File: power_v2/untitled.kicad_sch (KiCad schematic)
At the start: 15 parts, among them Q2 C1815_SOT23, U7 NEO-M8M

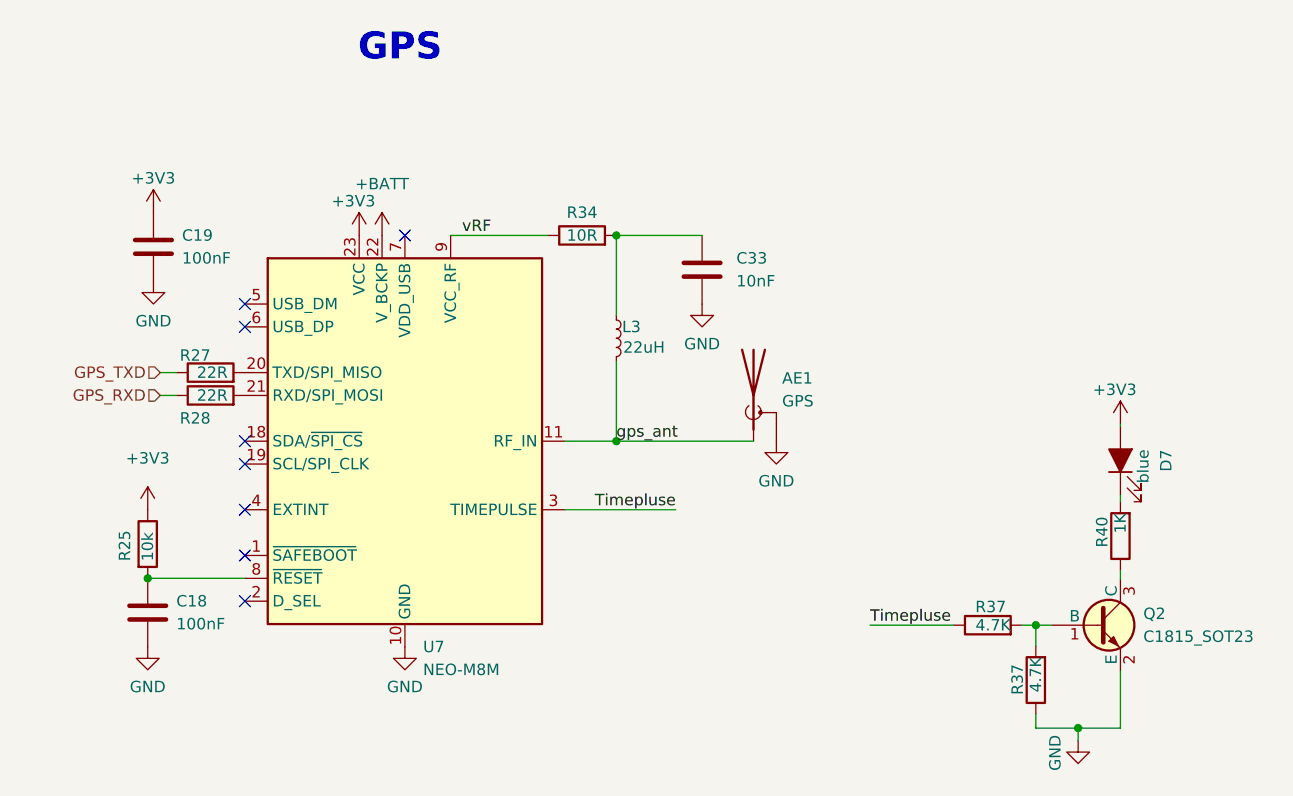
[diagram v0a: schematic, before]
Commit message: Modify tx/rx UART0, LED GPS, pin rst/clk sim card
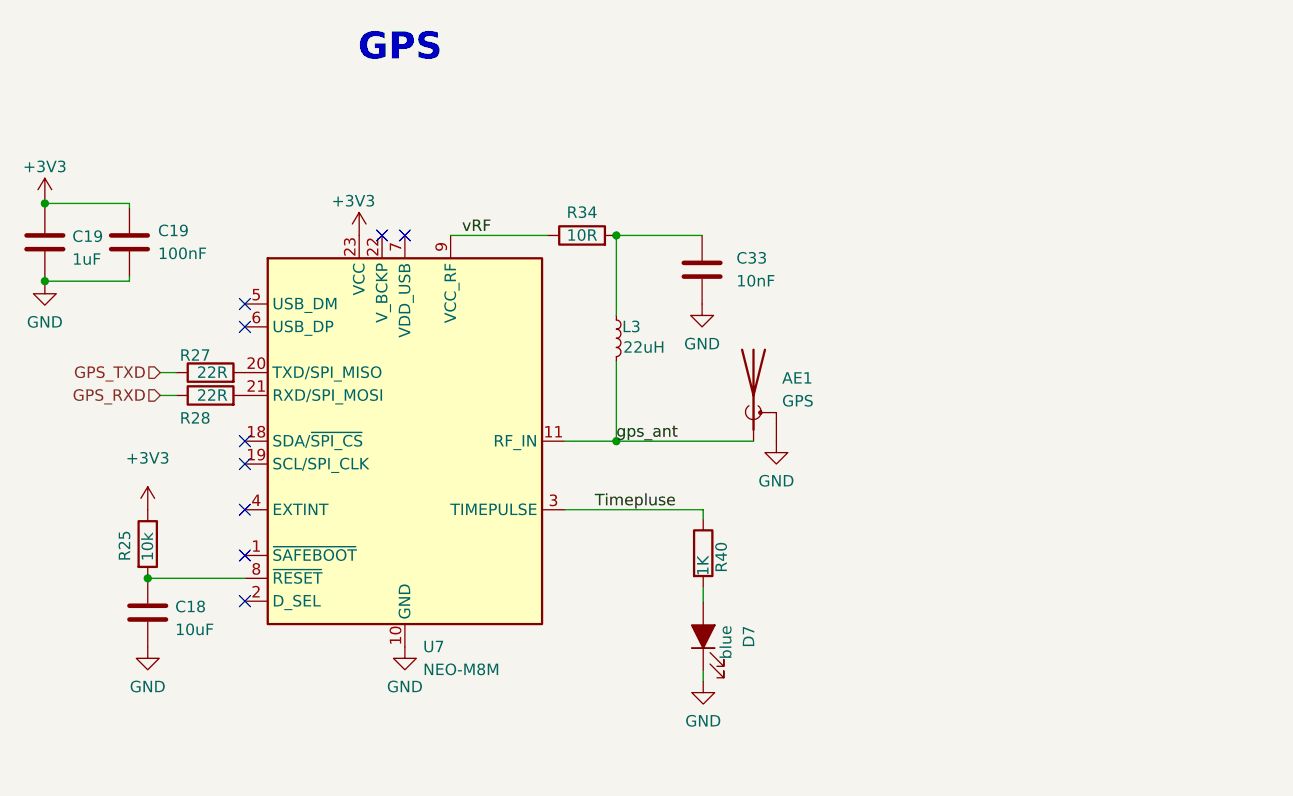
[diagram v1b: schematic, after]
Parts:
- removed Q2: C1815_SOT23, Package_TO_SOT_SMD:SOT-23, symbol ph_lib:C1815_SOT23
- removed R37 (x2): 4.7K, Resistor_SMD:R_0805_2012Metric, symbol ph_lib:R0805
- added C19: 100nF, Capacitor_SMD:C_0805_2012Metric, symbol ph_lib:C0805
- C18: value 100nF -> 10uF
- C19: value 100nF -> 1uF
- C33, L3, R34: footprint Resistor_SMD:R_0603_1608Metric -> Resistor_SMD:R_0805_2012Metric
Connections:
- net +3V3: now also C19.1; no longer D7.1 (A)
- net GND: now also D7.2 (K), C19.2
- net Timepluse: now also R40.1
- net at R40.2: now also D7.1 (A); no longer D7.2 (K)
- net +BATT: no longer names the net of U7.22 (V_BCKP)
- no-connect marks 8 -> 9
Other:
- moved on the sheet: C19, D7, R40
